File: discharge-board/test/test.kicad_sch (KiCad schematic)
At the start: 8 parts, among them J1 Screw_Terminal_01x02, J2 Screw_Terminal_01x02, J3 Screw_Terminal_01x02

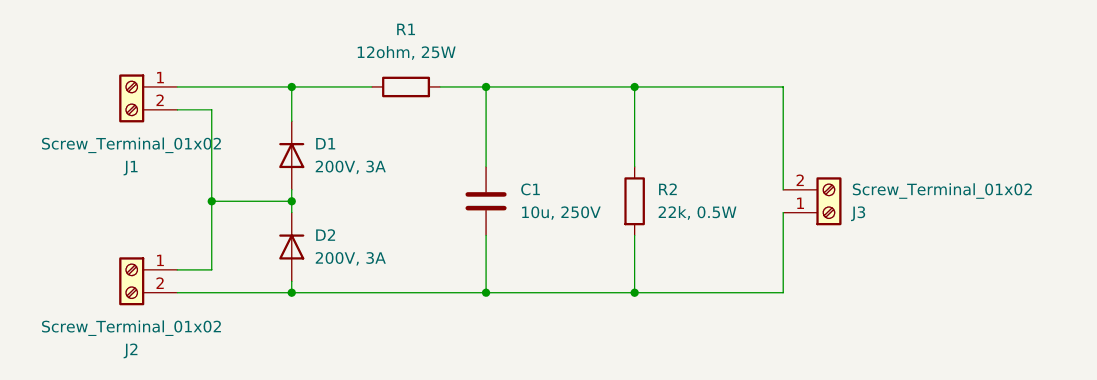
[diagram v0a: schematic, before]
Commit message: Decrease max current to 1.7A to prevent diode breakage
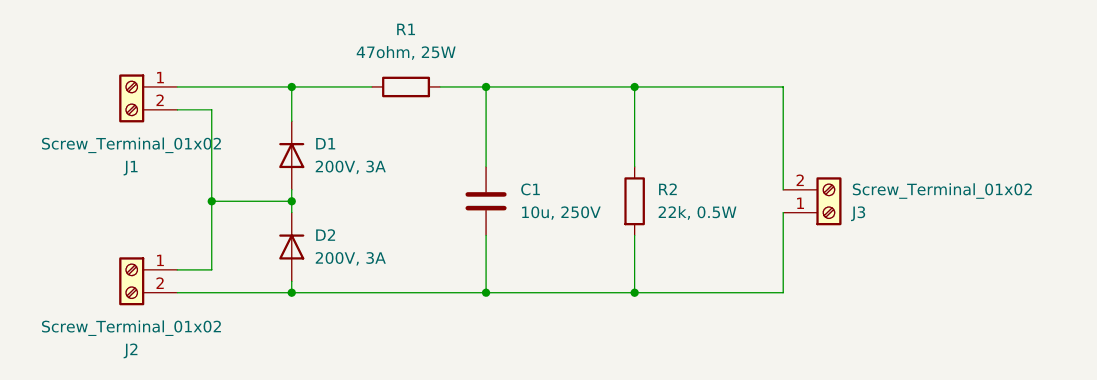
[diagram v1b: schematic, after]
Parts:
- R1: value 12ohm, 25W -> 47ohm, 25W
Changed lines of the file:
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@@
 			)
 		)
-		(property "Value" "12ohm, 25W"
+		(property "Value" "47ohm, 25W"
 			(at 102.87 43.18 90)
 			(effects
